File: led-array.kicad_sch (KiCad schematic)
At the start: 42 parts, among them J1 Conn_01x04_Pin, J2 USB_B_Micro, Q1 Q_NMOS_GDS, Q2 Q_NMOS_GDS, Q3 Q_NMOS_GDS, Q4 Q_NMOS_GDS, Q5 Q_NMOS_GDS, Q6 Q_NMOS_GDS, Q7 Q_NMOS_GDS, Q8 Q_NMOS_GDS, U1 TPS54331DR, U2 STM32F103C8T6, Y1 16MHz

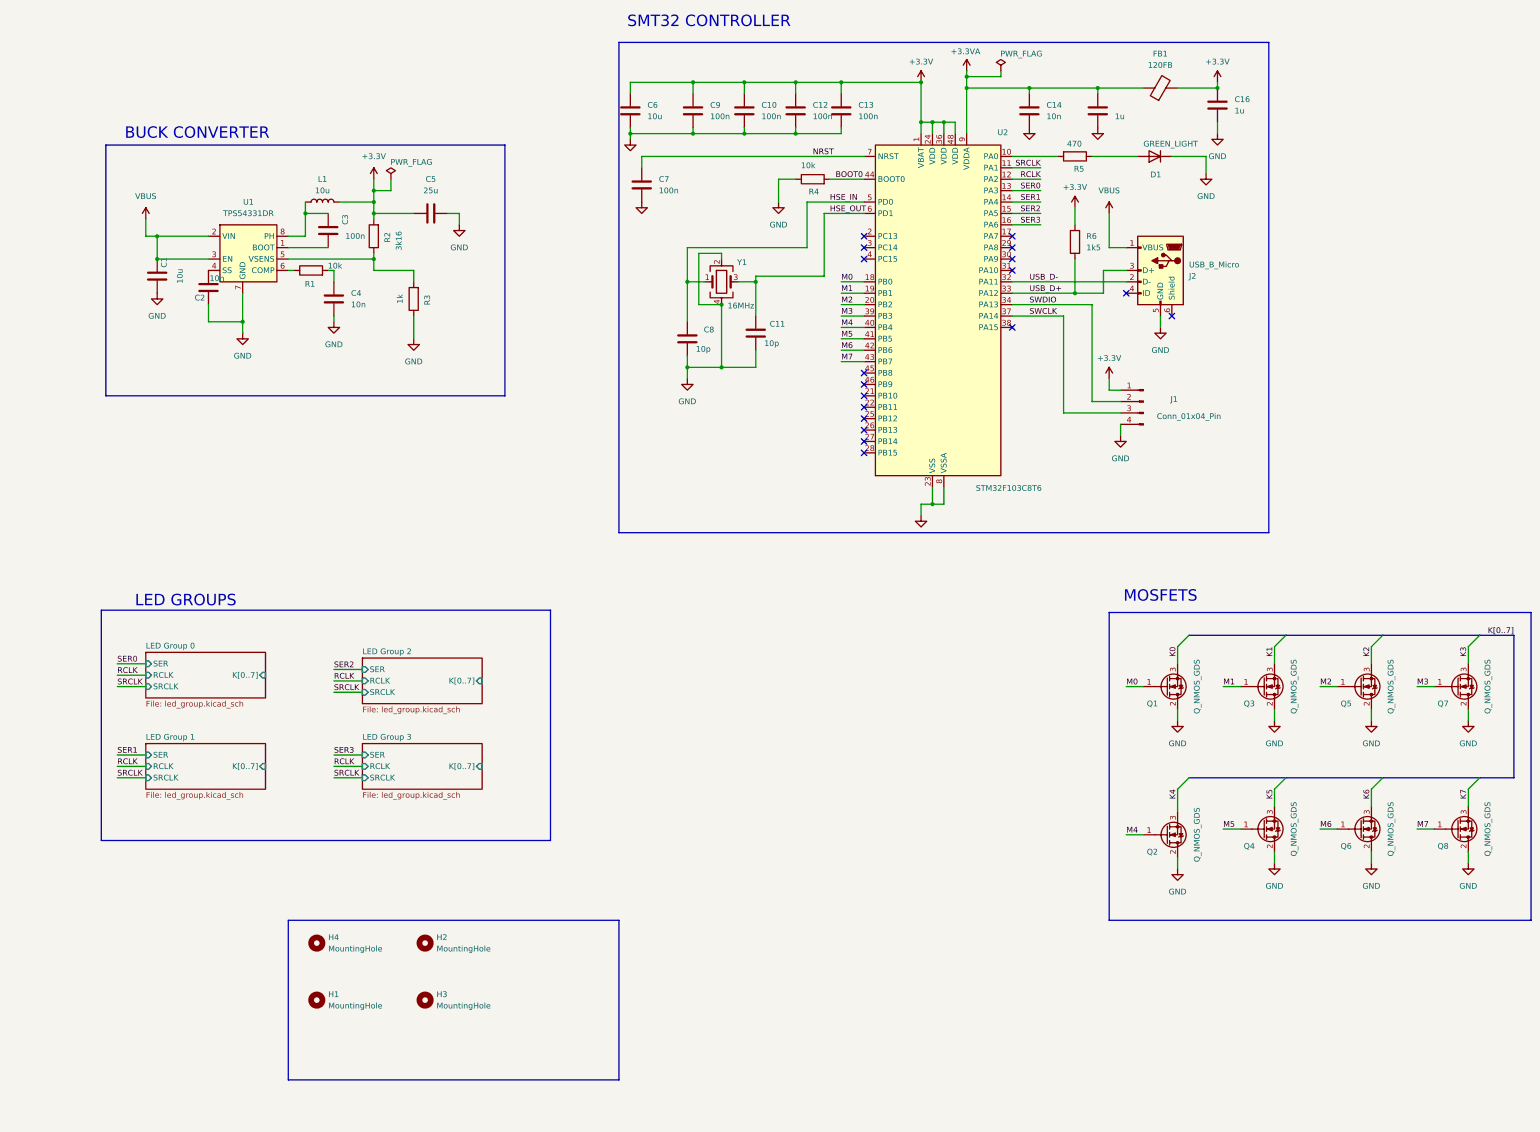
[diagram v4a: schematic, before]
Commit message: Relabeled MOSFETs
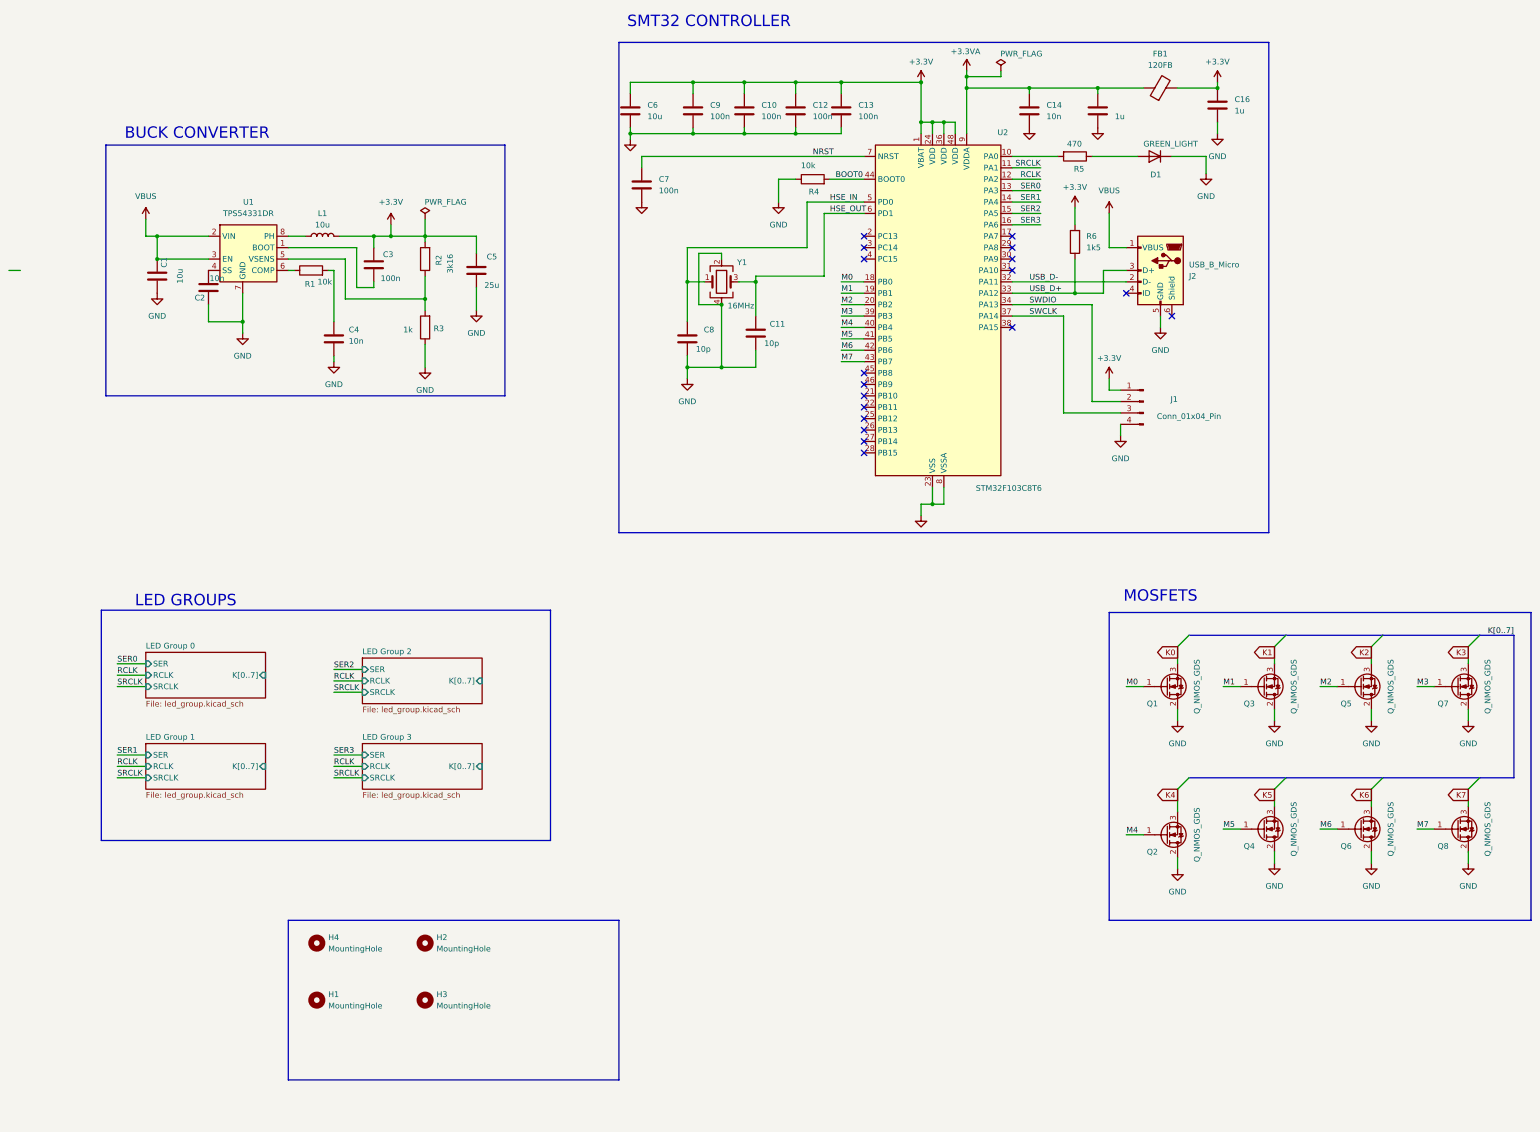
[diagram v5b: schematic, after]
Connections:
- net +3.3V: now also C3.1, C5.1; no longer C5.2
- net GND: now also C5.2; no longer C5.1
- net at L1.1, U1.8 (PH): no longer C3.1
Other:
- moved on the sheet: C3, C4, C5, L1, R2, R3

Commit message: Everything wired up
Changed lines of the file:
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@@
 	)
 	(junction
+		(at 100.33 73.66)
+		(diameter 0)
+		(color 0 0 0 0)
+	)
+	(junction
 		(at 173.99 50.8)
 		(diameter 0)
@@
 	)
 	(junction
-		(at 83.82 73.66)
-		(diameter 0)
-		(color 0 0 0 0)
-	)
-	(junction
 		(at 241.3 40.64)
 		(diameter 0)
@@
 	(wire
 		(pts
-			(xy 83.82 71.12) (xy 83.82 73.66)
+			(xy 100.33 71.12) (xy 100.33 73.66)
 		)
 		(stroke
@@
 	(wire
 		(pts
-			(xy 80.01 73.66) (xy 83.82 73.66)
+			(xy 80.01 73.66) (xy 91.44 73.66)
 		)
 		(stroke
@@
 	(wire
 		(pts
-			(xy 139.7 58.42) (xy 139.7 55.88)
+			(xy 100.33 73.66) (xy 91.44 73.66)
 		)
 		(stroke
@@
 	(wire
 		(pts
-			(xy 162.56 49.53) (xy 162.56 50.8)
+			(xy 139.7 58.42) (xy 139.7 55.88)
 		)
 		(stroke
@@
 	(wire
 		(pts
-			(xy 173.99 39.37) (xy 184.15 39.37)
+			(xy 162.56 49.53) (xy 162.56 50.8)
 		)
 		(stroke
@@
 	(wire
 		(pts
-			(xy 302.26 165.1) (xy 302.26 168.91)
+			(xy 173.99 39.37) (xy 184.15 39.37)
 		)
 		(stroke
@@
 	(wire
 		(pts
-			(xy 149.86 83.82) (xy 149.86 92.71)
+			(xy 302.26 165.1) (xy 302.26 168.91)
 		)
 		(stroke
@@
 	(wire
 		(pts
-			(xy 102.87 73.66) (xy 102.87 77.47)
+			(xy 149.86 83.82) (xy 149.86 92.71)
 		)
 		(stroke
@@
 	(wire
 		(pts
-			(xy 71.12 170.18) (xy 77.47 170.18)
+			(xy 102.87 73.66) (xy 102.87 77.47)
 		)
 		(stroke
@@
 	(wire
 		(pts
-			(xy 71.12 172.72) (xy 77.47 172.72)
+			(xy 71.12 170.18) (xy 77.47 170.18)
 		)
 		(stroke
@@
 	(wire
 		(pts
-			(xy 91.44 73.66) (xy 102.87 73.66)
+			(xy 71.12 172.72) (xy 77.47 172.72)
 		)
 		(stroke
@@
 	(wire
 		(pts
+			(xy 100.33 73.66) (xy 102.87 73.66)
+		)
+		(stroke
+			(width 0)
+			(type default)
+		)
+	)
+	(wire
+		(pts
 			(xy 184.15 41.91) (xy 184.15 39.37)
 		)
@@
 		)
 	)
-	(wire
-		(pts
-			(xy 83.82 73.66) (xy 91.44 73.66)
-		)
-		(stroke
-			(width 0)
-			(type default)
-		)
-	)
 	(bus
 		(pts
@@
 		)
 		(property "Value" "PWR_FLAG"
-			(at 96.012 66.04 0)
+			(at 89.916 65.532 0)
 			(effects
 				(font
@@
 	(symbol
 		(lib_id "power:+3.3V")
-		(at 83.82 71.12 0)
+		(at 100.33 71.12 0)
 		(unit 1)
 		(exclude_from_sim no)
@@
 		(fields_autoplaced yes)
 		(property "Reference" "#PWR04"
-			(at 83.82 74.93 0)
+			(at 100.33 74.93 0)
 			(effects
 				(font
@@
 		)
 		(property "Value" "+3.3V"
-			(at 83.82 66.04 0)
+			(at 100.33 66.04 0)
 			(effects
 				(font
@@
 		)
 		(property "Footprint" ""
-			(at 83.82 71.12 0)
+			(at 100.33 71.12 0)
 			(effects
 				(font
@@
 		)
 		(property "Datasheet" ""
-			(at 83.82 71.12 0)
+			(at 100.33 71.12 0)
 			(effects
 				(font
@@
 		)
 		(property "Description" "Power symbol creates a global label with name \"+3.3V\""
-			(at 83.82 71.12 0)
+			(at 100.33 71.12 0)
 			(effects
 				(font
